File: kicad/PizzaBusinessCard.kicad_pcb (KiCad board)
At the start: 2 copper layers, 86 x 54 mm, 16 parts, among them SW1 ON / OFF, U1 4017

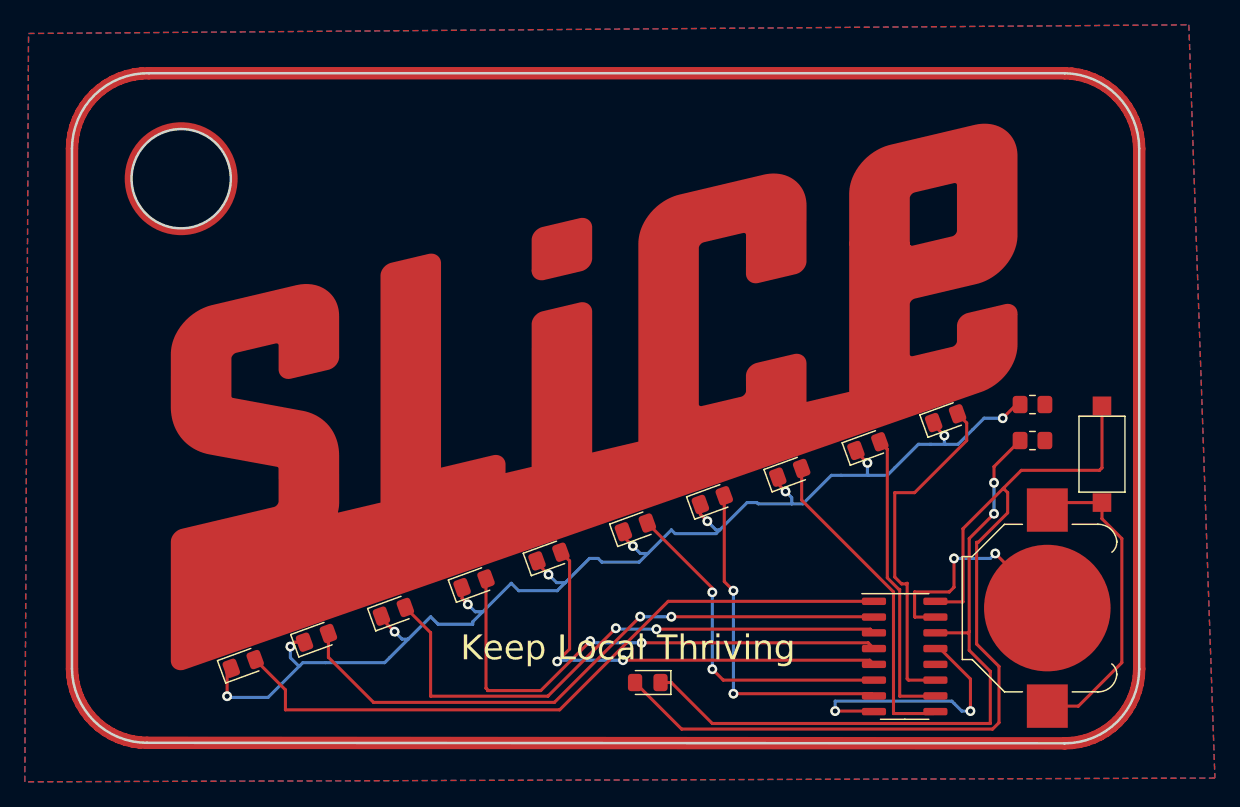
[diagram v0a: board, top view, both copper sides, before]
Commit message: implement with NE555
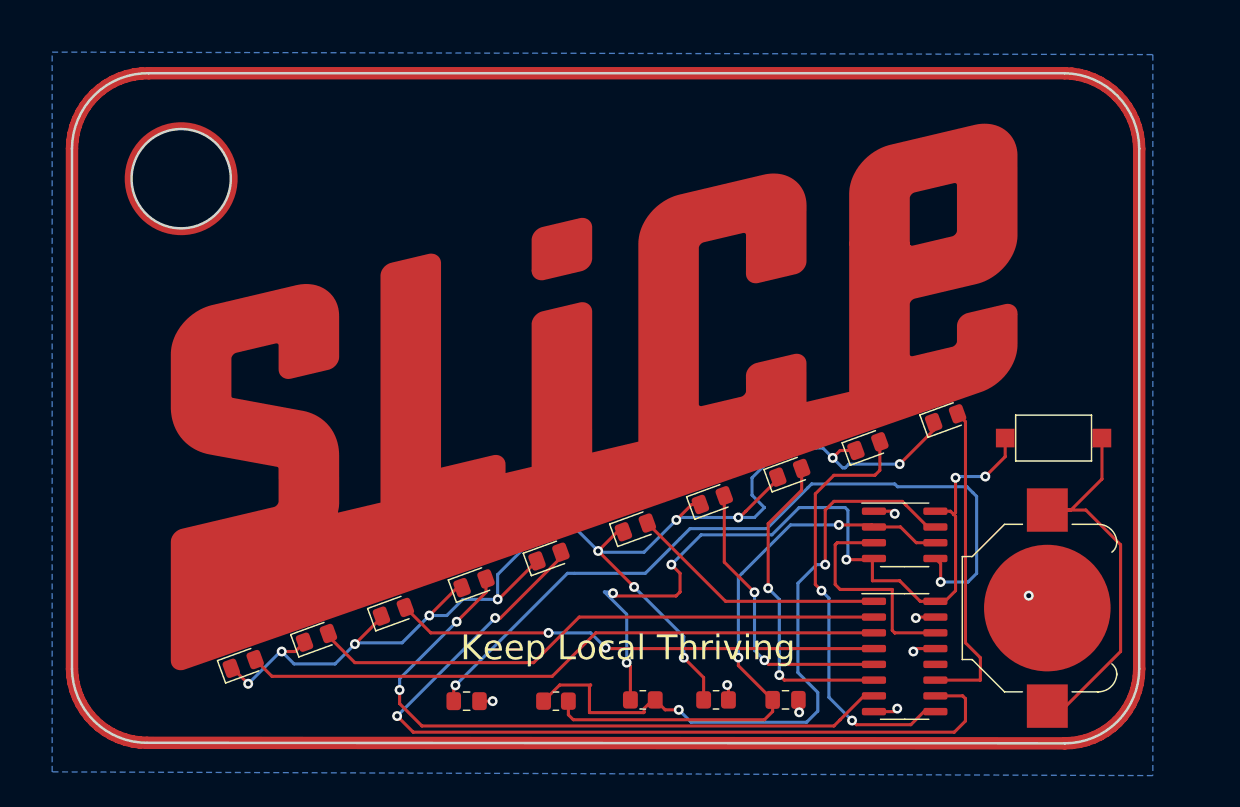
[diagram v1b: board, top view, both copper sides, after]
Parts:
- removed D1: LED, LED_SMD:LED_0805_2012Metric_Pad1.15x1.40mm_HandSolder
- added C1: 10nF, Capacitor_SMD:C_0805_2012Metric_Pad1.18x1.45mm_HandSolder, F.Cu at (115.0, 128.2)
- added C2: 10uF, Capacitor_SMD:C_0805_2012Metric_Pad1.18x1.45mm_HandSolder, F.Cu at (140.7, 128.1)
- added R3: 10K, Resistor_SMD:R_0805_2012Metric_Pad1.20x1.40mm_HandSolder, F.Cu at (122.2, 128.2)
- added U2: NE555D, Package_SO:SOIC-8_3.9x4.9mm_P1.27mm, F.Cu at (150.3, 114.8)
- R1: value 470 -> 10K
- moved R1 37.7 mm to (129.2, 128.1)
- moved R2 34.9 mm to (135.1, 128.1)
- moved SW1 4.11 mm to (162.3, 107.0), turned to 180 degrees
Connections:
- D10 pad 2: LED10 -> LED9
- D11 pad 2: LED11 -> LED10
- D9 pad 2: LED9 -> LED8
- R1 pad 1: GND -> Net-(R1-Pad1)
- R1 pad 2: LED_RGB -> 5V
- SW1 pad 2: BUTTON -> 5V
- U1 pad 1: LED1 -> LED6
- U1 pad 10: LED10 -> LED5
- U1 pad 11: LED11 -> LED10
- U1 pad 14: LED_RGB -> CLOCK
- U1 pad 16: BUTTON -> 5V
- U1 pad 3: LED3 -> LED1
- U1 pad 4: LED4 -> LED3
- U1 pad 5: LED5 -> LED7
- U1 pad 6: LED6 -> LED8
- U1 pad 7: LED7 -> LED4
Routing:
- net BUTTON: track 78.4 -> 0.00 mm
- net 5V: track 0.00 -> 67.5 mm, vias 0 -> 6
- net Net-(C1-Pad1): track 0.00 -> 61.9 mm, vias 0 -> 2
- net LED_RGB: track 55.9 -> 0.00 mm, vias 2 -> 0
- net Net-(R1-Pad1): track 0.00 -> 54.9 mm, vias 0 -> 2
- net Net-(C2-Pad1): track 0.00 -> 48.2 mm, vias 0 -> 2
- net LED5: track 35.2 -> 69.9 mm
- net GND: track 40.6 -> 12.5 mm, vias 4 -> 8
- net LED11: track 28.1 -> 0.00 mm
- net LED8: track 0.00 -> 25.9 mm, vias 0 -> 2
- net CLOCK: track 0.00 -> 18.0 mm
- net Net-(D10-Pad1): track 103.1 -> 114.7 mm, vias 11 -> 12
- net LED4: track 42.1 -> 52.9 mm
- net LED9: track 26.3 -> 35.1 mm, vias 0 -> 2
- net LED3: track 46.1 -> 39.1 mm
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- removed copper zone on F.Cu, net GND

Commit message: simplify ne555
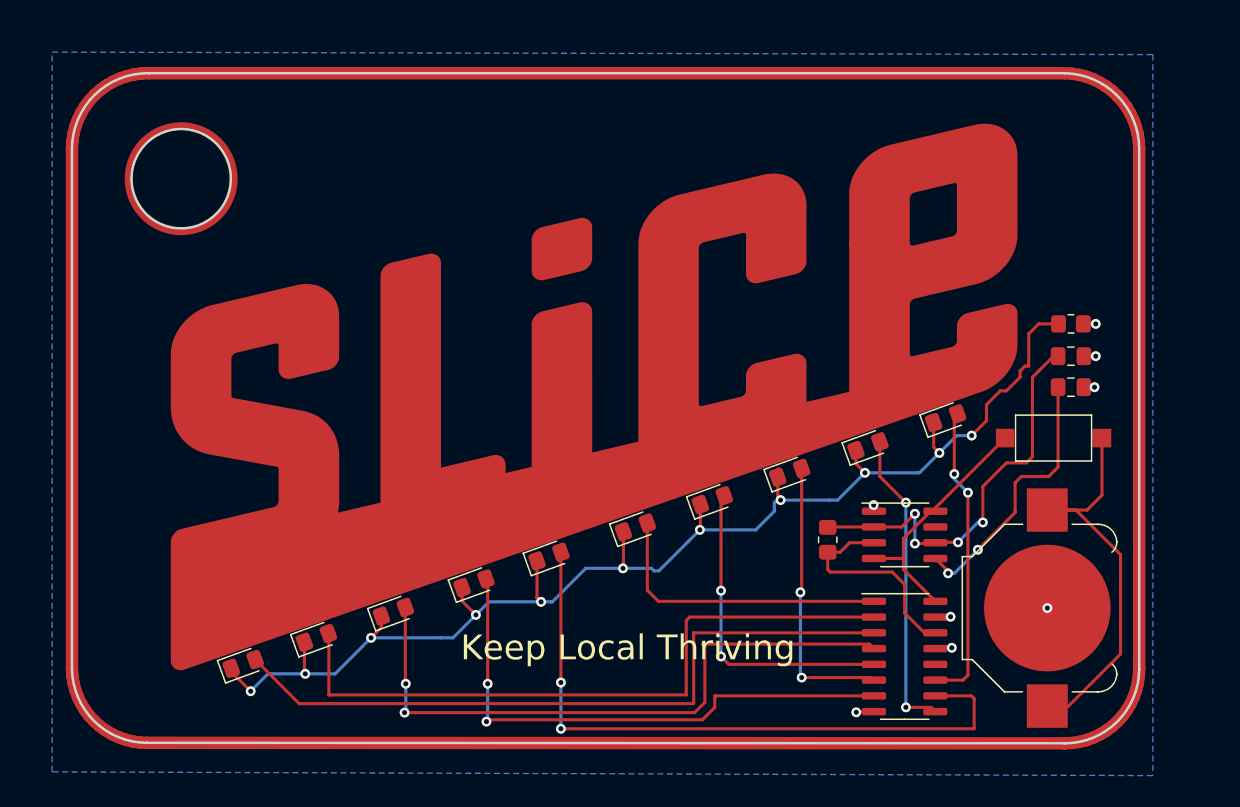
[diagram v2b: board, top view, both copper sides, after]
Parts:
- removed R1: 10K, Resistor_SMD:R_0805_2012Metric_Pad1.20x1.40mm_HandSolder
- C1: value 10nF -> 100nF
- C2: value 10uF -> 220nF
- moved C1 54.9 mm to (163.7, 102.9), turned to 180 degrees
- moved R2 41.7 mm to (163.7, 97.8)
- moved C2 36.0 mm to (163.7, 100.4)
- moved R3 25.5 mm to (144.1, 115.2), turned to -90 degrees
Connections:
- C1 pad 1: Net-(C1-Pad1) -> GND
- C1 pad 2: GND -> Net-(U2-Pad5)
- R3 pad 2: Net-(R1-Pad1) -> CLOCK
- U2 pad 5: Net-(C1-Pad1) -> Net-(U2-Pad5)
- U2 pad 7: Net-(R1-Pad1) -> unconnected-(U2-Pad7)
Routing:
- net Net-(C1-Pad1): track 61.9 -> 0.00 mm, vias 2 -> 0
- net Net-(R1-Pad1): track 54.9 -> 0.00 mm, vias 2 -> 0
- net 5V: track 67.5 -> 20.2 mm, vias 6 -> 0
- net Net-(U2-Pad5): track 0.00 -> 21.9 mm, vias 0 -> 2
- net LED5: track 69.9 -> 53.2 mm
- net Net-(R3-Pad1): track 48.2 -> 33.1 mm, vias 2 -> 4
- net LED3: track 39.1 -> 51.8 mm
- net LED9: track 35.1 -> 24.8 mm
- net Net-(D10-Pad1): track 114.7 -> 105.5 mm, vias 12 -> 11
- net LED4: track 52.9 -> 44.2 mm
- net LED2: track 46.6 -> 55.0 mm
- net LED1: track 51.9 -> 57.0 mm
- net GND: track 12.5 -> 7.37 mm
- net LED6: track 20.9 -> 24.0 mm
- net LED8: track 25.9 -> 22.8 mm
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
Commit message: fix ne555
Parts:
- removed C1: 100nF, Capacitor_SMD:C_0805_2012Metric_Pad1.18x1.45mm_HandSolder
- added R1: 10K, Resistor_SMD:R_0805_2012Metric_Pad1.20x1.40mm_HandSolder, F.Cu at (163.7, 100.7)
- C2: value 220nF -> 10uF
- moved R3 23.0 mm to (163.7, 103.2), turned to 0 degrees
- moved C2 2.30 mm to (163.7, 98.1)
- moved R2 2.30 mm to (163.7, 95.5)
- moved SW1 0.61 mm to (162.4, 107.6)
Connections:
- R3 pad 2: CLOCK -> Net-(R3-Pad2)
- U2 pad 5: Net-(U2-Pad5) -> unconnected-(U2-Pad5)
- U2 pad 7: unconnected-(U2-Pad7) -> Net-(R3-Pad2)
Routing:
- net Net-(C2-Pad1): track 33.1 -> 59.8 mm, vias 4 -> 0
- net Net-(U2-Pad5): track 21.9 -> 0.00 mm, vias 2 -> 0
- net Net-(R3-Pad2): track 0.00 -> 21.4 mm
- net LED9: track 24.8 -> 40.8 mm
- net 5V: track 20.2 -> 36.1 mm
- net LED10: track 24.4 -> 37.1 mm
- net LED3: track 51.8 -> 39.2 mm
- net LED2: track 55.0 -> 47.2 mm
- net Net-(D10-Pad1): track 105.5 -> 111.8 mm
- net LED8: track 22.8 -> 27.7 mm
- net LED1: track 57.0 -> 52.6 mm
- net LED4: track 44.2 -> 40.3 mm
- net VCC: track 32.5 -> 29.2 mm
- net LED5: track 53.2 -> 49.8 mm
- net LED6: track 24.0 -> 21.9 mm
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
